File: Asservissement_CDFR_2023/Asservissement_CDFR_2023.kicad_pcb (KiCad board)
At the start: 2 copper layers, 19 parts, among them IC1 A3930KJPTR-T, Q1 QM6006D, Q2 QM6006D, Q3 QM6006D, Q4 QM6006D, Q5 QM6006D, Q6 QM6006D, U1 LM317_TO-263, U2 LM317_TO-263, U3 STM32F401RCTx

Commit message: driver set up
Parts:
- U1, U2: value LM317_TO-263 -> LM317_SOT-223; footprint Package_TO_SOT_SMD:TO-263-2 -> Package_TO_SOT_SMD:SOT-223-3_TabPin2
- moved U1 12.2 mm to (85.1, 81.9)
- moved U2 3.64 mm to (95.0, 81.9)
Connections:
- IC1 pad 19: unconnected-(IC1-Pad19) -> Info_Courant_1

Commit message: schematic finished
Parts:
- added C10: 220u, Capacitor_SMD:CP_Elec_10x10.5, F.Cu at (74.6, 84.1)
- added C11: 100u, Capacitor_SMD:CP_Elec_10x10.5, F.Cu at (91.6, 73.7)
- added C12: 47nF, Capacitor_SMD:C_0805_2012Metric_Pad1.18x1.45mm_HandSolder, F.Cu at (137.4, 82.8)
- added C13: 47nF, Capacitor_SMD:C_0805_2012Metric_Pad1.18x1.45mm_HandSolder, F.Cu at (158.4, 66.8)
- added C14: 10pF, Capacitor_SMD:C_0805_2012Metric_Pad1.18x1.45mm_HandSolder, F.Cu at (96.2, 111.8)
- added C15: 10pF, Capacitor_SMD:C_0805_2012Metric_Pad1.18x1.45mm_HandSolder, F.Cu at (105.8, 113.0)
- added C16: 470nF, Capacitor_SMD:C_0805_2012Metric_Pad1.18x1.45mm_HandSolder, F.Cu at (149.7, 73.3)
- added C17: 10uF, Capacitor_SMD:C_0805_2012Metric_Pad1.18x1.45mm_HandSolder, F.Cu at (108.5, 110.0)
- added C18: 100nF, Capacitor_SMD:C_0805_2012Metric_Pad1.18x1.45mm_HandSolder, F.Cu at (90.4, 112.4)
- added C19: 1uF, Capacitor_SMD:C_0805_2012Metric_Pad1.18x1.45mm_HandSolder, F.Cu at (139.7, 79.5)
- added C20: 1uF, Capacitor_SMD:C_0805_2012Metric_Pad1.18x1.45mm_HandSolder, F.Cu at (149.7, 70.3)
- added C21: 220uF, Capacitor_SMD:CP_Elec_10x10.5, F.Cu at (79.3, 61.7)
- added C22: 47nF, Capacitor_SMD:C_0805_2012Metric_Pad1.18x1.45mm_HandSolder, F.Cu at (139.7, 76.5)
- added C23: 47nF, Capacitor_SMD:C_0805_2012Metric_Pad1.18x1.45mm_HandSolder, F.Cu at (163.1, 60.1)
- added C24: 47nF, Capacitor_SMD:C_0805_2012Metric_Pad1.18x1.45mm_HandSolder, F.Cu at (154.5, 70.3)
- added C25: 10nF, Capacitor_SMD:C_0805_2012Metric_Pad1.18x1.45mm_HandSolder, F.Cu at (101.0, 111.8)
- added C26: 1uF, Capacitor_SMD:C_0805_2012Metric_Pad1.18x1.45mm_HandSolder, F.Cu at (163.1, 57.1)
- added C7: 220u, Capacitor_SMD:CP_Elec_10x10.5, F.Cu at (96.2, 53.9)
- added C8: 100nF, Capacitor_SMD:C_0805_2012Metric_Pad1.18x1.45mm_HandSolder, F.Cu at (137.4, 85.8)
- added C9: 47nF, Capacitor_SMD:C_0805_2012Metric_Pad1.18x1.45mm_HandSolder, F.Cu at (167.9, 57.1)
- added CT1: 470pF, Capacitor_SMD:C_0805_2012Metric_Pad1.18x1.45mm_HandSolder, F.Cu at (144.5, 76.5)
- added CT2: 470pF, Capacitor_SMD:C_0805_2012Metric_Pad1.18x1.45mm_HandSolder, F.Cu at (114.8, 107.5)
- added D1: LED, LED_SMD:LED_0805_2012Metric_Pad1.15x1.40mm_HandSolder, F.Cu at (119.7, 106.6)
- added D2: LED, LED_SMD:LED_0805_2012Metric_Pad1.15x1.40mm_HandSolder, F.Cu at (110.6, 113.1)
- added D3: LED, LED_SMD:LED_0805_2012Metric_Pad1.15x1.40mm_HandSolder, F.Cu at (137.4, 88.9)
- added D4: LED, LED_SMD:LED_0805_2012Metric_Pad1.15x1.40mm_HandSolder, F.Cu at (149.7, 76.4)
- added D5: D_Zener, Diode_SMD:D_SOD-123, F.Cu at (90.9, 109.3)
- added IC2: A3930KJPTR-T, A3930KJPTR-T:A3930KJPTRT, F.Cu at (87.2, 100.9)
- added J1: Connecteur batterie, TerminalBlockBend:CUI_TBP01R1-508-02BE, F.Cu at (71.3, 100.9)
- added J10: Free Connecteur, Connector_PinHeader_2.54mm:PinHeader_1x08_P2.54mm_Vertical, F.Cu at (69.5, 50.2)
- added J11: Conn_01x02, Connector_JST:JST_XH_B2B-XH-A_1x02_P2.50mm_Vertical, F.Cu at (126.3, 93.0)
- added J12: Conn_01x02, Connector_JST:JST_XH_B2B-XH-A_1x02_P2.50mm_Vertical, F.Cu at (171.4, 51.2)
- added J13: Connecteur Odométrie, Connector_JST:JST_XH_B4B-XH-A_1x04_P2.50mm_Vertical, F.Cu at (104.3, 63.3)
- added J2: Conn_01x03, TerminalBlockBend:CUI_TBP02R1-381-03BE, F.Cu at (121.0, 56.6)
- added J3: Conn_01x05, Connector_JST:JST_XH_B5B-XH-A_1x05_P2.50mm_Vertical, F.Cu at (70.7, 73.6)
- added J4: Connecteur Programmation, Connector_PinHeader_2.54mm:PinHeader_1x04_P2.54mm_Vertical, F.Cu at (98.5, 82.1)
- added J5: Conn_01x03, Connector_PinHeader_2.54mm:PinHeader_1x03_P2.54mm_Vertical, F.Cu at (158.3, 58.0)
- added J6: Connecteur Odométrie, Connector_JST:JST_XH_B4B-XH-A_1x04_P2.50mm_Vertical, F.Cu at (89.9, 63.3)
- added J7: Conn_01x03, Connector_JST:JST_XH_B3B-XH-A_1x03_P2.50mm_Vertical, F.Cu at (159.5, 51.2)
- added J8: Conn_01x03, TerminalBlockBend:CUI_TBP02R1-381-03BE, F.Cu at (101.8, 76.5)
- added J9: Conn_01x05, Connector_JST:JST_XH_B5B-XH-A_1x05_P2.50mm_Vertical, F.Cu at (75.3, 51.2)
- added JP1: Jumper_3_Open, Connector_PinHeader_2.54mm:PinHeader_1x03_P2.54mm_Vertical, F.Cu at (120.5, 91.7)
- added L1: MDA4020-3R3M, Inductor_SMD:L_Vishay_IFSC-1515AH_4x4x1.8mm, F.Cu at (115.3, 100.2)
- added Q10: QM6006D, Package_TO_SOT_SMD:TO-252-2, F.Cu at (134.8, 68.0)
- added Q11: QM6006D, Package_TO_SOT_SMD:TO-252-2, F.Cu at (137.8, 51.9)
- added Q12: QM6006D, Package_TO_SOT_SMD:TO-252-2, F.Cu at (107.0, 83.4)
- added Q13: Q_NMOS_GDS, Package_TO_SOT_SMD:TO-252-2, F.Cu at (100.0, 106.3)
- added Q7: QM6006D, Package_TO_SOT_SMD:TO-252-2, F.Cu at (73.3, 108.6)
- added Q8: QM6006D, Package_TO_SOT_SMD:TO-252-2, F.Cu at (119.1, 77.3)
- added Q9: QM6006D, Package_TO_SOT_SMD:TO-252-2, F.Cu at (112.1, 93.4)
- added R10: 10k, Resistor_SMD:R_0805_2012Metric_Pad1.20x1.40mm_HandSolder, F.Cu at (159.2, 75.7)
- added R11: R, Resistor_SMD:R_0805_2012Metric_Pad1.20x1.40mm_HandSolder, F.Cu at (179.8, 52.3)
- added R12: R, Resistor_SMD:R_0805_2012Metric_Pad1.20x1.40mm_HandSolder, F.Cu at (151.8, 82.3)
- added R13: R, Resistor_SMD:R_0805_2012Metric_Pad1.20x1.40mm_HandSolder, F.Cu at (167.9, 60.1)
- added R14: 560, Resistor_SMD:R_0805_2012Metric_Pad1.20x1.40mm_HandSolder, F.Cu at (139.4, 91.9)
- added R15: 560, Resistor_SMD:R_0805_2012Metric_Pad1.20x1.40mm_HandSolder, F.Cu at (159.3, 72.8)
- added R16: 560, Resistor_SMD:R_0805_2012Metric_Pad1.20x1.40mm_HandSolder, F.Cu at (172.6, 63.0)
- added R17: 0.018, Resistor_SMD:R_2512_6332Metric, F.Cu at (83.7, 110.0)
- added R18: 56k, Resistor_SMD:R_0805_2012Metric_Pad1.20x1.40mm_HandSolder, F.Cu at (134.7, 94.8)
- added R19: 10k, Resistor_SMD:R_0805_2012Metric_Pad1.20x1.40mm_HandSolder, F.Cu at (179.8, 49.3)
- added R20: 220, Resistor_SMD:R_0805_2012Metric_Pad1.20x1.40mm_HandSolder, F.Cu at (164.0, 69.0)
- added R21: 10k, Resistor_SMD:R_0805_2012Metric_Pad1.20x1.40mm_HandSolder, F.Cu at (147.0, 82.5)
- added R22: 220, Resistor_SMD:R_0805_2012Metric_Pad1.20x1.40mm_HandSolder, F.Cu at (167.9, 66.0)
- added R23: 560, Resistor_SMD:R_0805_2012Metric_Pad1.20x1.40mm_HandSolder, F.Cu at (115.4, 110.5)
- added R24: 560, Resistor_SMD:R_0805_2012Metric_Pad1.20x1.40mm_HandSolder, F.Cu at (163.1, 66.1)
- added R25: 560, Resistor_SMD:R_0805_2012Metric_Pad1.20x1.40mm_HandSolder, F.Cu at (172.7, 60.1)
- added R26: R, Resistor_SMD:R_0805_2012Metric_Pad1.20x1.40mm_HandSolder, F.Cu at (134.8, 97.8)
- added R27: R, Resistor_SMD:R_0805_2012Metric_Pad1.20x1.40mm_HandSolder, F.Cu at (172.7, 57.1)
- added R28: R, Resistor_SMD:R_0805_2012Metric_Pad1.20x1.40mm_HandSolder, F.Cu at (125.3, 101.8)
- added R29: 560, Resistor_SMD:R_0805_2012Metric_Pad1.20x1.40mm_HandSolder, F.Cu at (124.4, 106.6)
- added R30: 560, Resistor_SMD:R_0805_2012Metric_Pad1.20x1.40mm_HandSolder, F.Cu at (125.3, 98.9)
- added R31: 560, Resistor_SMD:R_0805_2012Metric_Pad1.20x1.40mm_HandSolder, F.Cu at (154.4, 76.3)
- added R32: 0.018, Resistor_SMD:R_2512_6332Metric, F.Cu at (151.6, 66.4)
- added R33: 56k, Resistor_SMD:R_0805_2012Metric_Pad1.20x1.40mm_HandSolder, F.Cu at (120.1, 112.6)
- added R34: 4.7k, Resistor_SMD:R_0805_2012Metric_Pad1.20x1.40mm_HandSolder, F.Cu at (167.9, 63.1)
- added R35: 82k, Resistor_SMD:R_0805_2012Metric_Pad1.20x1.40mm_HandSolder, F.Cu at (177.4, 57.1)
- added R36: 10k, Resistor_SMD:R_0805_2012Metric_Pad1.20x1.40mm_HandSolder, F.Cu at (139.4, 94.8)
- added R37: 4.7, Resistor_SMD:R_0805_2012Metric_Pad1.20x1.40mm_HandSolder, F.Cu at (124.9, 109.5)
- added R38: 2.2k, Resistor_SMD:R_0805_2012Metric_Pad1.20x1.40mm_HandSolder, F.Cu at (147.0, 88.4)
- added R39: 2.2, Resistor_SMD:R_0805_2012Metric_Pad1.20x1.40mm_HandSolder, F.Cu at (129.2, 104.8)
- added R4: 3k9, Resistor_SMD:R_0805_2012Metric_Pad1.20x1.40mm_HandSolder, F.Cu at (115.4, 113.4)
- added R40: 82k, Resistor_SMD:R_0805_2012Metric_Pad1.20x1.40mm_HandSolder, F.Cu at (130.0, 98.9)
- added R41: 10k, Resistor_SMD:R_0805_2012Metric_Pad1.20x1.40mm_HandSolder, F.Cu at (163.1, 63.1)
- added R42: 50k, Resistor_SMD:R_0805_2012Metric_Pad1.20x1.40mm_HandSolder, F.Cu at (134.7, 91.9)
- added R5: 560, Resistor_SMD:R_0805_2012Metric_Pad1.20x1.40mm_HandSolder, F.Cu at (147.0, 85.5)
- added R6: 560, Resistor_SMD:R_0805_2012Metric_Pad1.20x1.40mm_HandSolder, F.Cu at (142.2, 88.5)
- added R7: 560, Resistor_SMD:R_0805_2012Metric_Pad1.20x1.40mm_HandSolder, F.Cu at (154.4, 79.2)
- added R8: 3.3k, Resistor_SMD:R_0805_2012Metric_Pad1.20x1.40mm_HandSolder, F.Cu at (154.4, 73.3)
- added R9: 220, Resistor_SMD:R_0805_2012Metric_Pad1.20x1.40mm_HandSolder, F.Cu at (159.3, 69.8)
- added RT1: 56k, Resistor_SMD:R_0805_2012Metric_Pad1.20x1.40mm_HandSolder, F.Cu at (142.2, 85.5)
- added RT2: 56k, Resistor_SMD:R_0805_2012Metric_Pad1.20x1.40mm_HandSolder, F.Cu at (149.3, 79.4)
- added RV1: 10k, Potentiometer_THT:Potentiometer_Bourns_3386C_Horizontal, F.Cu at (144.1, 66.9)
- added RV2: 10k, Potentiometer_THT:Potentiometer_Bourns_3386C_Horizontal, F.Cu at (109.2, 100.4)
- added Y1: Crystal_GND24, Crystal:Crystal_SMD_2520-4Pin_2.5x2.0mm, F.Cu at (184.4, 49.9)
- C1: value 0,1 uF -> 470nF
- C2: value 0,1 uF -> 10uF
- C3: value 1 uF -> 100nF
- C4: value 1 uF -> 1uF
- C5: value C -> 1uF
- C6: value C -> 220uF; footprint Capacitor_SMD:C_0805_2012Metric_Pad1.18x1.45mm_HandSolder -> Capacitor_SMD:CP_Elec_10x10.5
- R1: value R -> 1k
- R2: value R -> 2k4
- R3: value R -> 150
- U2: value LM317_SOT-223 -> TPS562200; footprint Package_TO_SOT_SMD:SOT-223-3_TabPin2 -> Package_TO_SOT_SMD:SOT-23-6
- moved C2 48.2 mm to (144.5, 79.5)
- moved U1 45.1 mm to (130.1, 85.5)
- moved C6 45.0 mm to (110.8, 53.9)
- moved Q3 36.5 mm to (100.0, 98.2)
- moved Q5 33.6 mm to (149.9, 51.9)
- moved Q6 33.6 mm to (149.9, 59.9)
- moved IC1 24.9 mm to (122.0, 66.6)
- moved U3 23.8 mm to (89.0, 87.0)
- moved R1 23.5 mm to (130.0, 101.8)
- moved C4 23.2 mm to (120.5, 103.6)
- moved R3 23.2 mm to (134.8, 100.7)
- moved Q1 21.4 mm to (119.1, 85.4)
- moved C5 19.3 mm to (114.8, 104.5)
- moved C3 18.6 mm to (120.5, 100.6)
- moved R2 18.5 mm to (120.1, 109.6)
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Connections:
- C1 pad 2: GND -> Net-(C1-Pad2)
- C2 pad 1: Net-(C1-Pad1) -> +BATT
- C3 pad 1: +5V -> +BATT
- C4 pad 1: +3.3V -> GND
- C4 pad 2: GND -> Net-(C4-Pad2)
- C5 pad 1: GND -> +BATT
- C5 pad 2: Net-(C5-Pad2) -> GND
- C6 pad 1: Net-(C6-Pad1) -> +BATT
- IC1 pad 24: VDRAIN -> +BATT
- IC1 pad 25: Net-(C12-Pad2) -> Net-(C13-Pad2)
- IC1 pad 28: Net-(C11-Pad2) -> Net-(C12-Pad2)
- IC1 pad 31: Net-(C10-Pad2) -> Net-(C9-Pad2)
- IC1 pad 39: action_fault -> action_fault_1
- IC1 pad 40: Net-(C9-Pad2) -> Net-(C4-Pad2)
- IC1 pad 42: Net-(C8-Pad2) -> Net-(C1-Pad2)
- IC1 pad 43: Net-(C8-Pad1) -> Net-(C1-Pad1)
- IC1 pad 44: dir_info_1 -> info_direction_1
- IC1 pad 45: VDRAIN -> +BATT
- IC1 pad 5: erreur_1_1 -> Info_erreur_1_1
- IC1 pad 6: erreur_2_1 -> Info_erreur_2_1
- IC1 pad 7: vitesse_1 -> Info_vitesse_1
- Q1 pad 2: VDRAIN -> +BATT
- Q1 pad 3: Net-(C12-Pad2) -> Net-(C13-Pad2)
- Q2 pad 2: Net-(C12-Pad2) -> +BATT
- Q2 pad 3: Net-(IC1-Pad22) -> Net-(C12-Pad2)
- Q3 pad 2: VDRAIN -> +BATT
- Q3 pad 3: Net-(C11-Pad2) -> Net-(C9-Pad2)
- Q4 pad 2: Net-(C11-Pad2) -> Net-(C13-Pad2)
- Q5 pad 2: VDRAIN -> Net-(C12-Pad2)
- Q5 pad 3: Net-(C10-Pad2) -> Net-(IC1-Pad22)
- Q6 pad 2: Net-(C10-Pad2) -> Net-(C9-Pad2)
- R1 pad 1: GND -> Net-(R1-Pad1)
- R1 pad 2: Net-(M1-Pad2) -> GND
- R2 pad 1: Net-(D1-Pad1) (its old number) -> +3.3V
- R2 pad 2: GND -> Net-(R2-Pad2)
- U1 pad 1: Net-(RV1-Pad2) -> Net-(R2-Pad2)
- U1 pad 2: +5V -> +3.3V
- U1 pad 3: Net-(C1-Pad1) -> +5V
- U2 pad 1: Net-(RV2-Pad2) -> GND
- U2 pad 2: +3.3V -> Net-(C8-Pad2)
- U2 pad 3: Net-(C1-Pad1) -> +BATT
- U3 pad 10: unconnected-(U3-Pad10) -> Net-(J10-Pad3)
- U3 pad 11: unconnected-(U3-Pad11) -> Net-(J10-Pad4)
- U3 pad 12: unconnected-(U3-Pad12) -> GND
- U3 pad 13: unconnected-(U3-Pad13) -> +5V
- U3 pad 14: unconnected-(U3-Pad14) -> Info_vitesse_1
- U3 pad 15: unconnected-(U3-Pad15) -> Info_vitesse_2
- U3 pad 16: unconnected-(U3-Pad16) -> /TX
- U3 pad 17: unconnected-(U3-Pad17) -> /RX
- U3 pad 2: unconnected-(U3-Pad2) -> reset_2
- U3 pad 20: unconnected-(U3-Pad20) -> Net-(R34-Pad1)
- U3 pad 21: unconnected-(U3-Pad21) -> Net-(R37-Pad1)
- U3 pad 22: unconnected-(U3-Pad22) -> Info_erreur_2_1
- U3 pad 23: unconnected-(U3-Pad23) -> Info_erreur_1_1
- U3 pad 24: unconnected-(U3-Pad24) -> Net-(J10-Pad5)
- U3 pad 25: unconnected-(U3-Pad25) -> Net-(J10-Pad6)
- U3 pad 26: unconnected-(U3-Pad26) -> Net-(J13-Pad2)
- U3 pad 27: unconnected-(U3-Pad27) -> Net-(J13-Pad3)
- U3 pad 28: unconnected-(U3-Pad28) -> Net-(J6-Pad2)
- U3 pad 29: unconnected-(U3-Pad29) -> frein_1
- U3 pad 3: unconnected-(U3-Pad3) -> disable_2
- U3 pad 33: unconnected-(U3-Pad33) -> frein_2
- U3 pad 35: unconnected-(U3-Pad35) -> Net-(J12-Pad2)
- U3 pad 36: unconnected-(U3-Pad36) -> Net-(J11-Pad2)
- U3 pad 37: unconnected-(U3-Pad37) -> Net-(J10-Pad7)
- U3 pad 38: unconnected-(U3-Pad38) -> Net-(J10-Pad8)
- U3 pad 39: unconnected-(U3-Pad39) -> action_fault_2
- U3 pad 4: unconnected-(U3-Pad4) -> disable_1
- U3 pad 40: unconnected-(U3-Pad40) -> action_fault_1
- U3 pad 41: unconnected-(U3-Pad41) -> Info_erreur_2_2
- U3 pad 42: unconnected-(U3-Pad42) -> Info_erreur_1_2
- U3 pad 43: unconnected-(U3-Pad43) -> info_direction_1
- U3 pad 44: unconnected-(U3-Pad44) -> info_direction_2
- U3 pad 45: unconnected-(U3-Pad45) -> Net-(D3-Pad2)
- U3 pad 46: unconnected-(U3-Pad46) -> SWDIO
- U3 pad 49: unconnected-(U3-Pad49) -> SWCLK
- U3 pad 5: Net-(C5-Pad2) -> Net-(C14-Pad2)
- U3 pad 50: unconnected-(U3-Pad50) -> Net-(D4-Pad2)
- U3 pad 51: unconnected-(U3-Pad51) -> MODE_2
- U3 pad 52: unconnected-(U3-Pad52) -> MODE_1
- U3 pad 53: unconnected-(U3-Pad53) -> reset_1
- U3 pad 55: unconnected-(U3-Pad55) -> Net-(J6-Pad3)
- U3 pad 56: unconnected-(U3-Pad56) -> speed_controle_1
- U3 pad 57: unconnected-(U3-Pad57) -> speed_controle_2
- U3 pad 58: unconnected-(U3-Pad58) -> /I2C_CLK
- U3 pad 59: unconnected-(U3-Pad59) -> /I2C_SDA
- U3 pad 6: Net-(C6-Pad1) -> Net-(C15-Pad1)
- U3 pad 60: unconnected-(U3-Pad60) -> Net-(R21-Pad2)
- U3 pad 61: unconnected-(U3-Pad61) -> direction_controle_2
- U3 pad 62: unconnected-(U3-Pad62) -> direction_controle_1
- U3 pad 8: unconnected-(U3-Pad8) -> Net-(J10-Pad1)
- U3 pad 9: unconnected-(U3-Pad9) -> Net-(J10-Pad2)

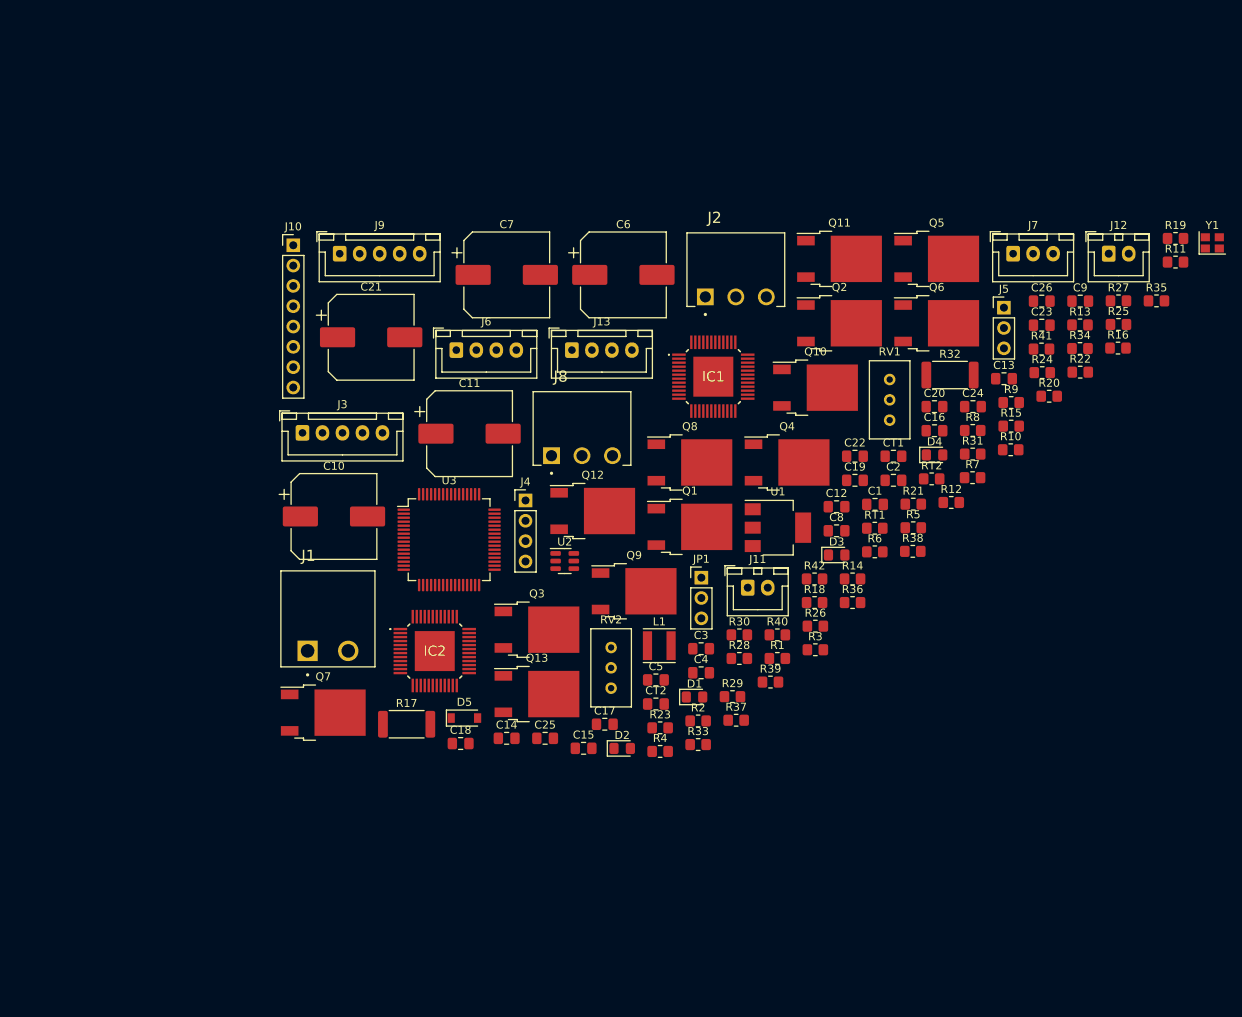
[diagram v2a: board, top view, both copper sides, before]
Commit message: Pré-routage carte asservissement (en attente de correctif sur l'ordre des pins du stm32)
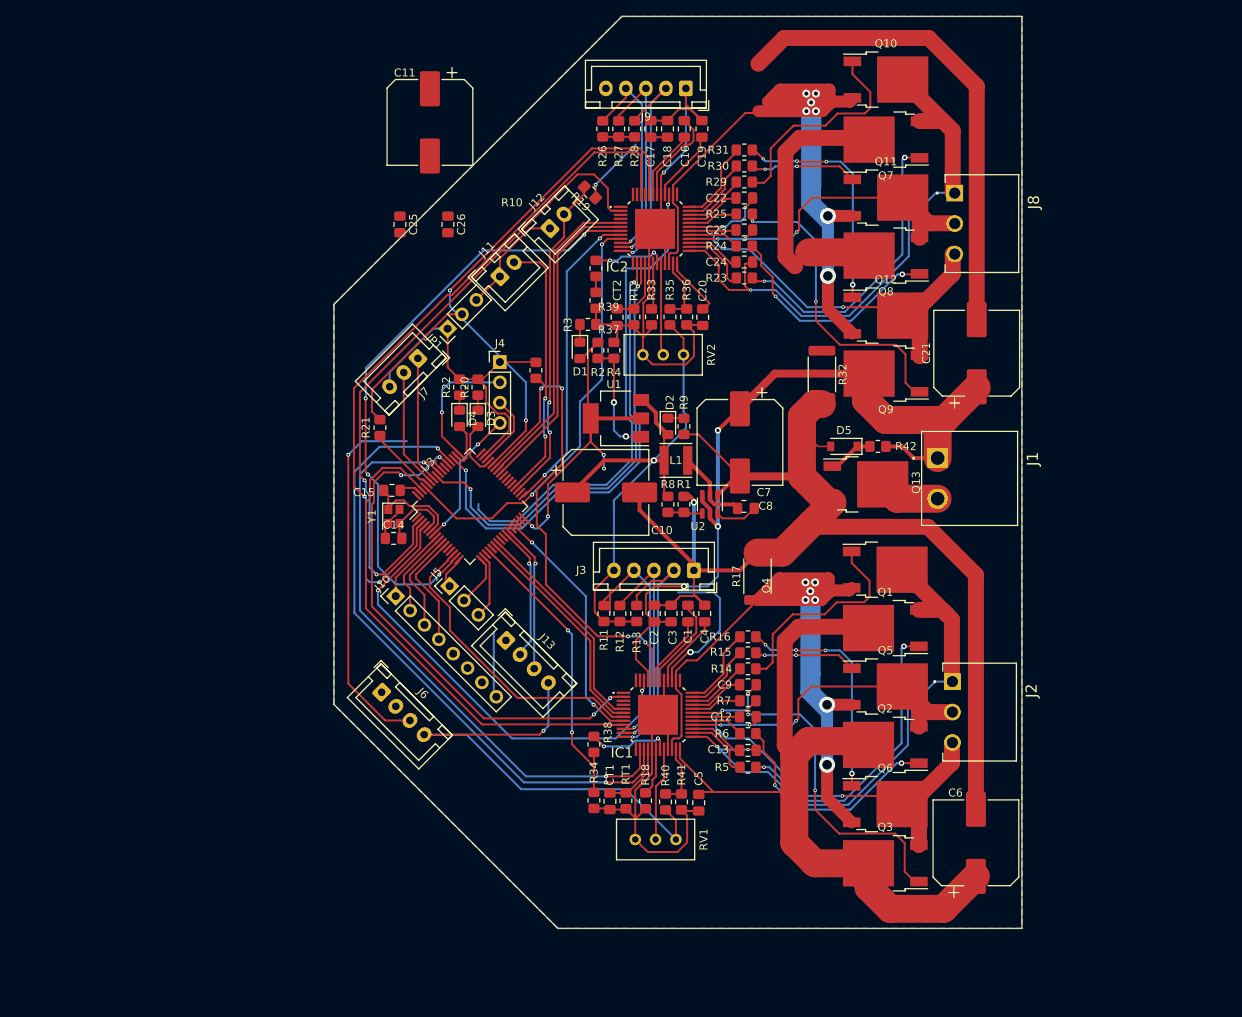
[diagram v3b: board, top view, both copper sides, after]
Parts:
- moved Y1 107.9 mm to (82.1, 84.0), turned to -90 degrees
- moved Q7 100.4 mm to (143.6, 37.0), turned to 180 degrees
- moved R11 83.9 mm to (108.3, 96.2), turned to 90 degrees
- moved C6 83.6 mm to (154.8, 124.8), turned to 90 degrees
- moved R34 83.0 mm to (107.1, 119.5), turned to -90 degrees
- moved J1 82.4 mm to (150.1, 76.8), turned to -90 degrees
- moved C18 81.1 mm to (116.3, 35.6), turned to 90 degrees
- moved R22 77.6 mm to (90.3, 67.9), turned to 90 degrees
- moved J5 77.5 mm to (89.1, 92.8), turned to 45 degrees
- moved C21 75.7 mm to (154.9, 63.6), turned to 90 degrees
- moved J7 75.5 mm to (85.1, 64.3), turned to -135 degrees
- moved C26 74.8 mm to (88.8, 47.5), turned to -90 degrees
- moved C17 74.6 mm to (114.2, 35.6), turned to 90 degrees
- moved R19 73.4 mm to (106.6, 43.5), turned to 135 degrees
- moved R41 72.3 mm to (118.0, 119.7), turned to -90 degrees
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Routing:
- net GND: track 0.00 -> 402.5 mm, vias 0 -> 3
- net +BATT: track 0.00 -> 241.6 mm, vias 0 -> 3
- net +5V: track 0.00 -> 142.1 mm, vias 0 -> 2
- net Net-(IC1-Pad22): track 0.00 -> 114.3 mm, vias 0 -> 7
- net Net-(IC2-Pad22): track 0.00 -> 111.8 mm, vias 0 -> 7
- net disable_2: track 0.00 -> 89.1 mm, vias 0 -> 2
- net reset_2: track 0.00 -> 80.3 mm, vias 0 -> 2
- net MODE_1: track 0.00 -> 80.1 mm, vias 0 -> 2
- net Info_vitesse_2: track 0.00 -> 76.7 mm, vias 0 -> 4
- net speed_controle_1: track 0.00 -> 74.5 mm, vias 0 -> 2
- net Net-(C24-Pad2): track 0.00 -> 71.9 mm, vias 0 -> 1
- net Net-(C13-Pad2): track 0.00 -> 70.7 mm, vias 0 -> 2
- net reset_1: track 0.00 -> 65.2 mm, vias 0 -> 4
- net info_direction_2: track 0.00 -> 64.8 mm, vias 0 -> 2
- net direction_controle_1: track 0.00 -> 62.8 mm
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- added copper zone on B.Cu, net GND
- added copper zone on F.Cu, net GND
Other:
- board outline added: 86 x 114 mm

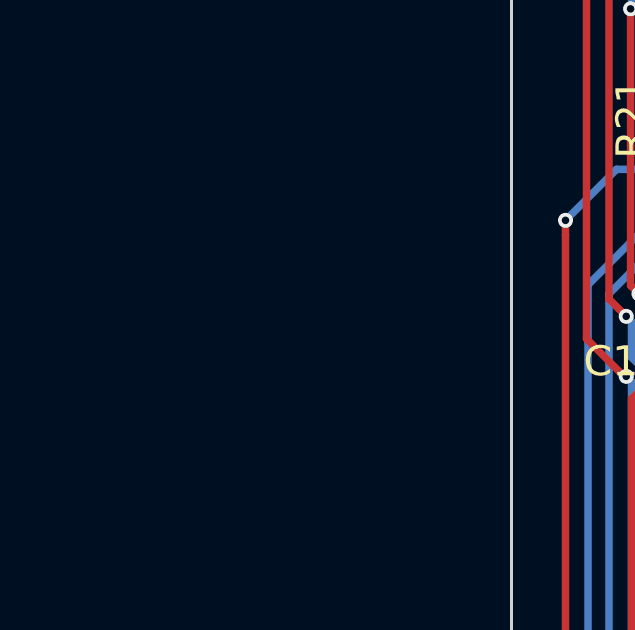
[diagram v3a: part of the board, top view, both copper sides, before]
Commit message: uController modification pinout
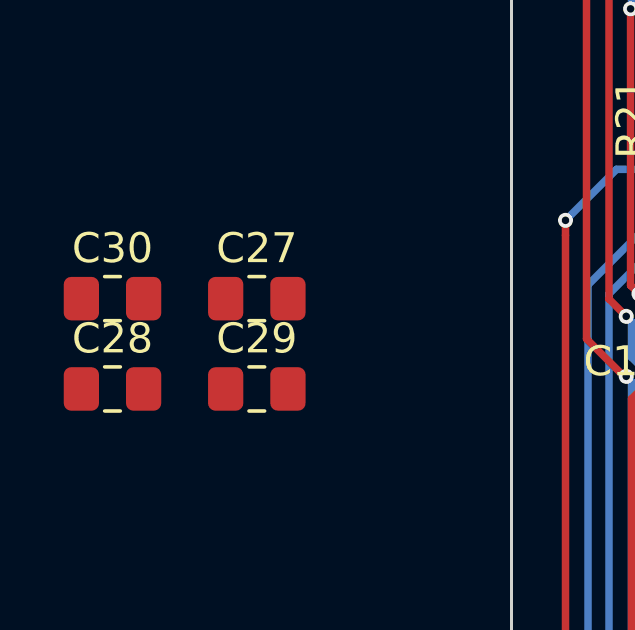
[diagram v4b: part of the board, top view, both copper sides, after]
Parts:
- added C27: 100n, Capacitor_SMD:C_0805_2012Metric_Pad1.18x1.45mm_HandSolder, F.Cu at (66.1, 79.0)
- added C28: 100n, Capacitor_SMD:C_0805_2012Metric_Pad1.18x1.45mm_HandSolder, F.Cu at (61.3, 82.0)
- added C29: 100n, Capacitor_SMD:C_0805_2012Metric_Pad1.18x1.45mm_HandSolder, F.Cu at (66.1, 82.0)
- added C30: 100n, Capacitor_SMD:C_0805_2012Metric_Pad1.18x1.45mm_HandSolder, F.Cu at (61.3, 79.0)
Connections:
- J10 pad 1: Net-(J10-Pad1) -> Free1
- J10 pad 2: Net-(J10-Pad2) -> Free2
- J10 pad 3: Net-(J10-Pad3) -> Free3
- J10 pad 4: Net-(J10-Pad4) -> Free4
- J10 pad 5: Net-(J10-Pad5) -> Free5
- J10 pad 6: Net-(J10-Pad6) -> Free6
- J10 pad 7: Net-(J10-Pad7) -> Free7
- J10 pad 8: Net-(J10-Pad8) -> Free8
- J13 pad 2: Net-(J13-Pad2) -> odometrie2
- J13 pad 3: Net-(J13-Pad3) -> Net-(U3-Pad55)
- J6 pad 2: Net-(J6-Pad2) -> Net-(U3-Pad56)
- J6 pad 3: Net-(J6-Pad3) -> Net-(U3-Pad57)
- R34 pad 1: Net-(R34-Pad1) -> Net-(U3-Pad15)
- R38 pad 1: Net-(R34-Pad1) -> Net-(U3-Pad15)
- U3 pad 10: Net-(J10-Pad3) -> Free7
- U3 pad 11: Net-(J10-Pad4) -> Free8
- U3 pad 14: Info_vitesse_1 -> MODE_1
- U3 pad 15: Info_vitesse_2 -> Net-(U3-Pad15)
- U3 pad 2: reset_2 -> Free2
- U3 pad 20: Net-(R34-Pad1) -> direction_controle_1
- U3 pad 21: Net-(R37-Pad1) -> Info_vitesse_1
- U3 pad 22: Info_erreur_2_1 -> frein_1
- U3 pad 23: Info_erreur_1_1 -> Info_erreur_2_1
- U3 pad 24: Net-(J10-Pad5) -> Info_erreur_1_1
- U3 pad 25: Net-(J10-Pad6) -> reset_1
- U3 pad 26: Net-(J13-Pad2) -> speed_controle_1
- U3 pad 27: Net-(J13-Pad3) -> disable_1
- U3 pad 28: Net-(J6-Pad2) -> info_direction_1
- U3 pad 29: frein_1 -> action_fault_1
- U3 pad 3: disable_2 -> Free3
- U3 pad 33: frein_2 -> MODE_2
- U3 pad 34: unconnected-(U3-Pad34) -> speed_controle_2
- U3 pad 35: Net-(J12-Pad2) -> direction_controle_2
- U3 pad 36: Net-(J11-Pad2) -> frein_2
- U3 pad 37: Net-(J10-Pad7) -> Info_vitesse_2
- U3 pad 38: Net-(J10-Pad8) -> Info_erreur_2_2
- U3 pad 39: action_fault_2 -> Info_erreur_1_2
- U3 pad 4: disable_1 -> Free4
- U3 pad 40: action_fault_1 -> reset_2
- U3 pad 41: Info_erreur_2_2 -> disable_2
- U3 pad 42: Info_erreur_1_2 -> info_direction_2
- U3 pad 43: info_direction_1 -> action_fault_2
- U3 pad 44: info_direction_2 -> Net-(R37-Pad1)
- U3 pad 51: MODE_2 -> unconnected-(U3-Pad51)
- U3 pad 52: MODE_1 -> Net-(J12-Pad2)
- U3 pad 53: reset_1 -> Net-(J11-Pad2)
- U3 pad 54: unconnected-(U3-Pad54) -> odometrie2
- U3 pad 55: Net-(J6-Pad3) -> Net-(U3-Pad55)
- U3 pad 56: speed_controle_1 -> Net-(U3-Pad56)
- U3 pad 57: speed_controle_2 -> Net-(U3-Pad57)
- U3 pad 61: direction_controle_2 -> unconnected-(U3-Pad61)
- U3 pad 62: direction_controle_1 -> Free1
- U3 pad 8: Net-(J10-Pad1) -> Free5
- U3 pad 9: Net-(J10-Pad2) -> Free6
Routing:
- net Net-(U3-Pad57): track 0.00 -> 103.6 mm, vias 0 -> 3
- net GND: track 402.5 -> 486.6 mm, vias 3 -> 5
- net Free1: track 0.00 -> 72.2 mm
- net info_direction_2: track 64.8 -> 0.00 mm, vias 2 -> 0
- net direction_controle_1: track 62.8 -> 0.00 mm
- net speed_controle_2: track 57.4 -> 0.00 mm, vias 2 -> 0
- net unconnected-(U3-Pad61): track 0.00 -> 53.8 mm, vias 0 -> 2
- net direction_controle_2: track 53.8 -> 0.00 mm, vias 2 -> 0
- net Net-(J6-Pad3): track 47.9 -> 0.00 mm, vias 1 -> 0
- net frein_2: track 39.0 -> 0.00 mm, vias 2 -> 0
- net MODE_2: track 58.5 -> 97.5 mm, vias 2 -> 4
- net Net-(U3-Pad15): track 0.00 -> 37.6 mm, vias 0 -> 2
- net Net-(R34-Pad1): track 37.6 -> 0.00 mm, vias 2 -> 0
- net Net-(U3-Pad55): track 0.00 -> 20.3 mm, vias 0 -> 1
- net Net-(JP1-Pad2): track 19.3 -> 0.00 mm
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
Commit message: capacitor error
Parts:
- removed C30: 100n, Capacitor_SMD:C_0805_2012Metric_Pad1.18x1.45mm_HandSolder
- moved C27 4.84 mm to (64.2, 83.4)
- moved C28 3.30 mm to (64.2, 80.4)
- moved C29 3.30 mm to (69.0, 80.4)
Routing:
- net reset_2: track 80.3 -> 0.00 mm, vias 2 -> 0
- net Free2: track 11.0 -> 91.2 mm, vias 0 -> 2
- net Net-(R34-Pad1): track 37.6 -> 114.3 mm, vias 2 -> 6
- net Info_vitesse_2: track 76.7 -> 0.00 mm, vias 4 -> 0
- net reset_1: track 65.2 -> 0.00 mm, vias 4 -> 0
- net Net-(J11-Pad2): track 35.9 -> 101.1 mm, vias 2 -> 6
- net info_direction_1: track 62.3 -> 0.00 mm, vias 4 -> 0
- net action_fault_2: track 61.1 -> 123.4 mm, vias 1 -> 5
- net speed_controle_2: track 0.00 -> 57.4 mm, vias 0 -> 2
- net Net-(J6-Pad3): track 103.6 -> 46.2 mm, vias 3 -> 1
- net info_direction_2: track 0.00 -> 40.0 mm
- net Info_erreur_1_2: track 40.0 -> 0.00 mm
- net frein_2: track 0.00 -> 39.0 mm, vias 0 -> 2
- net MODE_2: track 97.5 -> 58.5 mm, vias 4 -> 2
- net frein_1: track 31.1 -> 59.4 mm
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
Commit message: capacitor error
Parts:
- added C30: 100n, Capacitor_SMD:C_0805_2012Metric_Pad1.18x1.45mm_HandSolder, F.Cu at (69.3, 83.4)
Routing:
- net reset_2: track 0.00 -> 80.3 mm, vias 0 -> 2
- net Free2: track 91.2 -> 11.0 mm, vias 2 -> 0
- net Net-(R34-Pad1): track 114.3 -> 37.6 mm, vias 6 -> 2
- net Info_vitesse_2: track 0.00 -> 76.7 mm, vias 0 -> 4
- net Net-(J6-Pad2): track 0.00 -> 74.5 mm, vias 0 -> 2
- net info_direction_1: track 0.00 -> 62.3 mm, vias 0 -> 4
- net action_fault_2: track 123.4 -> 61.1 mm, vias 5 -> 1
- net disable_1: track 76.6 -> 18.6 mm, vias 3 -> 1
- net Free4: track 0.00 -> 58.0 mm, vias 0 -> 2
- net speed_controle_1: track 74.5 -> 17.3 mm, vias 2 -> 1
- net unconnected-(U3-Pad61): track 53.8 -> 0.00 mm, vias 2 -> 0
- net direction_controle_2: track 0.00 -> 53.8 mm, vias 0 -> 2
- net info_direction_2: track 40.0 -> 0.00 mm
- net Info_erreur_1_2: track 0.00 -> 40.0 mm
- net frein_1: track 59.4 -> 31.1 mm
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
